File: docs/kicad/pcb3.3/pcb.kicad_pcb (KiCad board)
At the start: 2 copper layers, 62.2 x 76.2 mm, 26 parts, among them J1 power, J2 coil1, J3 coil2, J5 Sensor, J8 leds, Q1 BC548, Q2 IRF9540N, SW1 SW, SW2 SW, U2 ESP32_DEV_0

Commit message: updated pcb3.3 (no plots, flatcam, or gcode)
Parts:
- added C2: 330uf, 0_my_footprints:CP_my100uf, F.Cu at (36.8, -6.35)
- moved Q1 41.5 mm to (6.35, -16.5), turned to 270 degrees
- moved R2 30.6 mm to (43.8, -57.1), turned to 0 degrees
- moved Q2 30.1 mm to (5.08, -39.4), turned to 90 degrees
- moved C1 28.2 mm to (8.89, -58.4)
- moved R9 22.9 mm to (8.89, -38.1), turned to 90 degrees
- moved J1 20.9 mm to (26.7, -61.0)
- moved R8 20.5 mm to (11.4, -21.6), turned to 270 degrees
- moved J2 11.7 mm to (12.7, -68.6), turned to 90 degrees
- moved D1 11.4 mm to (17.8, -63.5)
- moved J3 4.58 mm to (17.8, -68.6), turned to 90 degrees
- moved J8 0.86 mm to (48.9, -71.8)
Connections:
- J2 pad 2: COIL+ -> Net-(J2-Pad2)
- J3 pad 1: GND -> Net-(J2-Pad2)
- SW1 pad 1: GND -> SW1
- SW1 pad 2: SW1 -> GND
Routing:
- net PWM: track 22.6 -> 3.81 mm
- net +5V: track 84.9 -> 98.3 mm
- net SCL: track 44.2 -> 32.2 mm, vias 2 -> 0
- net Net-(Q1-Pad2): track 16.6 -> 5.08 mm
- net COIL+: track 29.7 -> 35.7 mm
- net Net-(Q1-Pad1): track 23.0 -> 28.5 mm
- net Net-(J2-Pad2): track 0.00 -> 4.30 mm
- net +3V3: track 61.2 -> 64.8 mm
- net SW1: track 27.2 -> 29.3 mm
- net VBAT: track 24.3 -> 25.8 mm
- net VBUS: track 69.0 -> 67.8 mm, vias 2 -> 0
- net GND: track 0.00 -> 0.98 mm
- net LEDS: track 32.6 -> 31.8 mm
- net S5V: track 15.8 -> 15.0 mm
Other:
- board text added: "The coils are wired with red to center and black to outside, They run in series, the back black to ground, reds connected together, and front's black to the coil voltage."
- board text added: "back black red"
- board text added: "front red black"
- board text added: "optional 3V capacitor laying under ESP32"

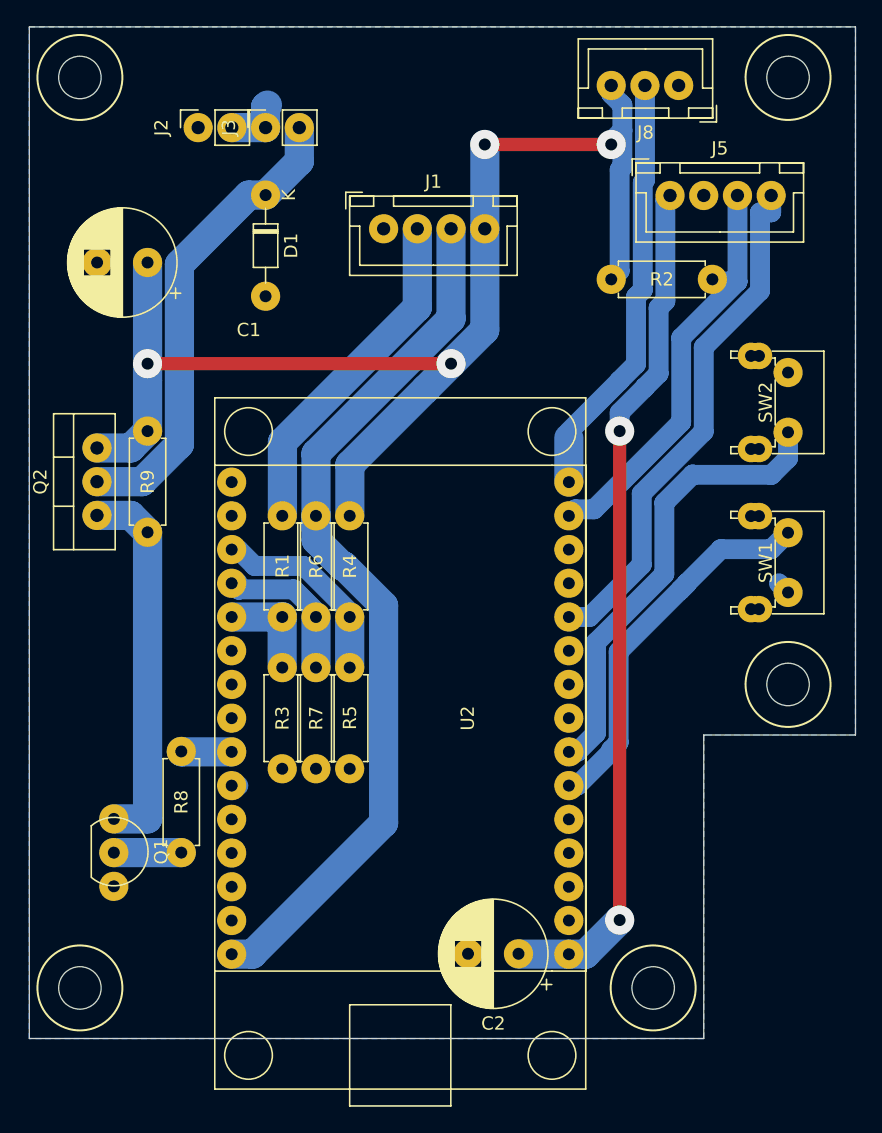
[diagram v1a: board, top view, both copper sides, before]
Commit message: Rework PCB3.3, import it into fusion, more documentation WIP
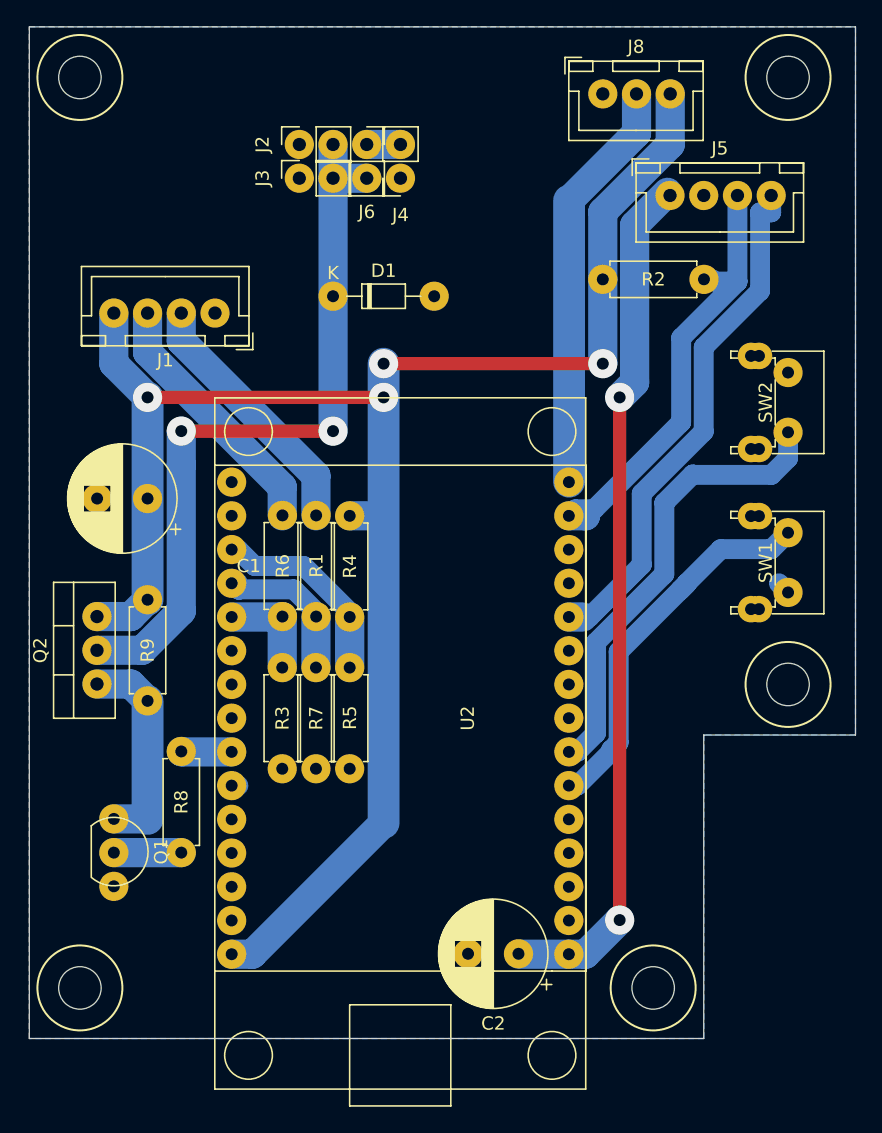
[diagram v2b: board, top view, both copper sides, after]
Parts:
- added J4: coil1, 0_my_footprints:myPinSocket_1x02, F.Cu at (27.9, -64.8)
- added J6: coil2, 0_my_footprints:myPinSocket_1x02, F.Cu at (25.4, -67.3)
- C2: value 330uf -> 100 uf
- moved C1 17.8 mm to (8.89, -40.6)
- moved J1 14.2 mm to (14.0, -54.6), turned to 180 degrees
- moved R9 12.7 mm to (8.89, -25.4)
- moved Q2 12.7 mm to (5.08, -26.7)
- moved D1 9.16 mm to (22.9, -55.9), turned to 0 degrees
- moved J2 7.73 mm to (20.3, -67.3)
- moved J8 5.75 mm to (43.2, -71.1), turned to 0 degrees
- moved J3 4.58 mm to (20.3, -64.8)
- moved R1 2.56 mm to (21.6, -31.8)
- moved R6 2.52 mm to (19.1, -31.8)
- moved R2 0.63 mm to (43.2, -57.1)
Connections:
- J2 pad 2: Net-(J2-Pad2) -> COIL+
- J3 pad 1: Net-(J2-Pad2) -> GND
- R3 pad 1: SBAT -> SBUS
- R7 pad 1: SBUS -> SBAT
- U2 pad 1: VBUS -> +5V
- U2 pad 11: SBAT -> SBUS
- U2 pad 12: SBUS -> SBAT
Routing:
- net VBUS: track 67.8 -> 19.5 mm
- net +5V: track 98.3 -> 136.4 mm
- net COIL+: track 35.7 -> 56.7 mm, vias 0 -> 2
- net Net-(Q1-Pad1): track 28.5 -> 15.8 mm
- net VBAT: track 25.8 -> 19.5 mm
- net SBUS: track 12.3 -> 7.67 mm
- net SBAT: track 7.67 -> 12.3 mm
- net Net-(J2-Pad2): track 4.30 -> 0.00 mm
- net Net-(J4-Pad2): track 0.00 -> 2.54 mm
- net SCL: track 32.2 -> 33.5 mm
- net SDA: track 39.5 -> 40.5 mm
- net +3V3: track 64.8 -> 65.5 mm
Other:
- board text added: "The coils can be connected in series or parallel. Parallel provides more power, but requires different parameters to avoid brownouts and reboots."
- board text added: "parallel"
- board text added: "series"
- board text removed: "The coils are wired with red to center and black to outside, They run in series, the back black to ground, reds connected together, and front's black to the coil voltage."
- board text removed: "back black red"
- board text removed: "front red black"
